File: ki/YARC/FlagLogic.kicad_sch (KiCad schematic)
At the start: 11 parts, among them U105 74LS86, U106 74LS139, U107 74HC00, U108 74HC02, U109 74LS32, U110 74LS21, U111 74LS153, U112 74LS573, U113 74LS573, U114 74LS574, U115 74LS574

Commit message: Various corrections and minor improvements
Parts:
- removed unit 4 of U107
- removed unit 3 of U107
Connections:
- net GND: now also U107.1; no longer U107.4, U107.5
- net IRH2: now also U107.4, U107.5; no longer U107.1, U107.2
- net at U111.1 (Ea): now also U107.6; no longer U107.3
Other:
- moved on the sheet: U107A
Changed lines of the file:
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@@
   (junction (at 40.64 119.38) (diameter 0) (color 0 0 0 0)
   )
-  (junction (at 33.02 172.72) (diameter 0) (color 0 0 0 0)
-  )
   (junction (at 86.36 165.1) (diameter 0) (color 0 0 0 0)
   )
@@
   (junction (at 76.2 172.72) (diameter 0) (color 0 0 0 0)
   )
-  (junction (at 33.02 180.34) (diameter 0) (color 0 0 0 0)
-  )
   (junction (at 30.48 45.72) (diameter 0) (color 0 0 0 0)
   )
   (junction (at 73.66 147.32) (diameter 0) (color 0 0 0 0)
   )
-  (junction (at 30.48 193.04) (diameter 0) (color 0 0 0 0)
-  )
   (junction (at 86.36 160.02) (diameter 0) (color 0 0 0 0)
   )
   (junction (at 53.34 147.32) (diameter 0) (color 0 0 0 0)
   )
-  (junction (at 50.8 193.04) (diameter 0) (color 0 0 0 0)
-  )
   (junction (at 121.92 172.72) (diameter 0) (color 0 0 0 0)
   )
@@
   (junction (at 33.02 48.26) (diameter 0) (color 0 0 0 0)
   )
-  (junction (at 50.8 172.72) (diameter 0) (color 0 0 0 0)
-  )
   (junction (at 76.2 193.04) (diameter 0) (color 0 0 0 0)
   )
@@
     (stroke (width 0) (type default) (color 0 0 0 0))
   )
-  (wire (pts (xy 30.48 198.12) (xy 30.48 193.04))
-    (stroke (width 0) (type default) (color 0 0 0 0))
-  )
   (bus (pts (xy 172.72 22.86) (xy 190.5 22.86))
     (stroke (width 0) (type default) (color 0 0 0 0))
@@
     (stroke (width 0) (type default) (color 0 0 0 0))
   )
-  (wire (pts (xy 30.48 193.04) (xy 30.48 172.72))
-    (stroke (width 0) (type default) (color 0 0 0 0))
-  )
   (wire (pts (xy 241.3 73.66) (xy 241.3 60.96))
     (stroke (width 0) (type default) (color 0 0 0 0))
@@
     (stroke (width 0) (type default) (color 0 0 0 0))
   )
-  (wire (pts (xy 30.48 172.72) (xy 33.02 172.72))
+  (wire (pts (xy 30.48 172.72) (xy 35.56 172.72))
     (stroke (width 0) (type default) (color 0 0 0 0))
   )
@@
     (stroke (width 0) (type default) (color 0 0 0 0))
   )
-  (wire (pts (xy 50.8 198.12) (xy 50.8 193.04))
-    (stroke (width 0) (type default) (color 0 0 0 0))
-  )
   (wire (pts (xy 25.4 119.38) (xy 40.64 119.38))
     (stroke (width 0) (type default) (color 0 0 0 0))
   )
+  (wire (pts (xy 30.48 180.34) (xy 30.48 172.72))
+    (stroke (width 0) (type default) (color 0 0 0 0))
+  )
   (wire (pts (xy 104.14 93.98) (xy 109.22 93.98))
     (stroke (width 0) (type default) (color 0 0 0 0))
   )
-  (wire (pts (xy 33.02 180.34) (xy 33.02 172.72))
-    (stroke (width 0) (type default) (color 0 0 0 0))
-  )
   (wire (pts (xy 73.66 172.72) (xy 76.2 172.72))
     (stroke (width 0) (type default) (color 0 0 0 0))
@@
     (stroke (width 0) (type default) (color 0 0 0 0))
   )
-  (wire (pts (xy 33.02 185.42) (xy 33.02 180.34))
-    (stroke (width 0) (type default) (color 0 0 0 0))
-  )
   (bus (pts (xy 228.6 88.9) (xy 246.38 88.9))
     (stroke (width 0) (type default) (color 0 0 0 0))
@@
     (stroke (width 0) (type default) (color 0 0 0 0))
   )
-  (wire (pts (xy 35.56 172.72) (xy 50.8 172.72))
+  (wire (pts (xy 35.56 172.72) (xy 53.34 172.72))
     (stroke (width 0) (type default) (color 0 0 0 0))
   )
@@
     (stroke (width 0) (type default) (color 0 0 0 0))
   )
-  (wire (pts (xy 50.8 193.04) (xy 50.8 172.72))
-    (stroke (width 0) (type default) (color 0 0 0 0))
-  )
   (wire (pts (xy 170.18 73.66) (xy 170.18 60.96))
     (stroke (width 0) (type default) (color 0 0 0 0))
@@
     (stroke (width 0) (type default) (color 0 0 0 0))
   )
-  (wire (pts (xy 50.8 172.72) (xy 53.34 172.72))
-    (stroke (width 0) (type default) (color 0 0 0 0))
-  )
   (wire (pts (xy 19.05 147.32) (xy 35.56 147.32))
     (stroke (width 0) (type default) (color 0 0 0 0))
@@
   )
   (bus (pts (xy 22.86 99.06) (xy 22.86 104.14))
-    (stroke (width 0) (type default) (color 0 0 0 0))
-  )
-  (wire (pts (xy 33.02 172.72) (xy 35.56 172.72))
     (stroke (width 0) (type default) (color 0 0 0 0))
   )
@@
     (pin "3")
   )
-  (symbol (lib_id "74xx:74HC00") (at 38.1 195.58 0) (unit 2)
-    (in_bom yes) (on_board yes)
-    (property "Reference" "U107" (id 0) (at 43.18 190.5 0))
-    (property "Value" "74HC00" (id 1) (at 38.1 195.58 0))
-    (property "Footprint" "" (id 2) (at 38.1 195.58 0)
-      (effects (font (size 1.27 1.27)) hide)
-    )
-    (property "Datasheet" "http://www.ti.com/lit/gpn/sn74hc00" (id 3) (at 38.1 195.58 0)
-      (effects (font (size 1.27 1.27)) hide)
-    )
-    (pin "4")
-    (pin "5")
-    (pin "6")
+  (symbol (lib_id "74xx:74HC00") (at 38.1 182.88 0) (unit 1)
+    (in_bom yes) (on_board yes)
+    (property "Reference" "U107" (id 0) (at 43.18 177.8 0))
+    (property "Value" "74HC00" (id 1) (at 38.1 182.88 0))
+    (property "Footprint" "" (id 2) (at 38.1 182.88 0)
+      (effects (font (size 1.27 1.27)) hide)
+    )
+    (property "Datasheet" "http://www.ti.com/lit/gpn/sn74hc00" (id 3) (at 38.1 182.88 0)
+      (effects (font (size 1.27 1.27)) hide)
+    )
+    (pin "1")
+    (pin "2")
+    (pin "3")
   )
   (symbol (lib_id "74xx:74HC02") (at 83.82 195.58 0) (unit 1)
@@
     (pin "9")
   )
-  (symbol (lib_id "74xx:74HC00") (at 53.34 73.66 0) (unit 1)
+  (symbol (lib_id "74xx:74HC00") (at 53.34 73.66 0) (unit 2)
     (in_bom yes) (on_board yes)
     (property "Reference" "U107" (id 0) (at 58.42 68.58 0))
@@
       (effects (font (size 1.27 1.27)) hide)
     )
-    (pin "1")
-    (pin "2")
-    (pin "3")
+    (pin "4")
+    (pin "5")
+    (pin "6")
   )
   (symbol (lib_id "74xx:74LS32") (at 129.54 60.96 270) (unit 2)
@@
     (pin "1")
   )
-  (symbol (lib_id "74xx:74HC00") (at 58.42 195.58 0) (unit 4)
-    (in_bom yes) (on_board yes)
-    (property "Reference" "U107" (id 0) (at 63.5 190.5 0))
-    (property "Value" "74HC00" (id 1) (at 58.42 195.58 0))
-    (property "Footprint" "" (id 2) (at 58.42 195.58 0)
-      (effects (font (size 1.27 1.27)) hide)
-    )
-    (property "Datasheet" "http://www.ti.com/lit/gpn/sn74hc00" (id 3) (at 58.42 195.58 0)
-      (effects (font (size 1.27 1.27)) hide)
-    )
-    (pin "11")
-    (pin "12")
-    (pin "13")
-  )
   (symbol (lib_id "74xx:74LS32") (at 73.66 160.02 0) (unit 5)
     (in_bom yes) (on_board yes)
@@
     (pin "1")
   )
-  (symbol (lib_id "74xx:74HC00") (at 40.64 182.88 0) (unit 3)
-    (in_bom yes) (on_board yes)
-    (property "Reference" "U107" (id 0) (at 45.72 177.8 0))
-    (property "Value" "74HC00" (id 1) (at 40.64 182.88 0))
-    (property "Footprint" "" (id 2) (at 40.64 182.88 0)
-      (effects (font (size 1.27 1.27)) hide)
-    )
-    (property "Datasheet" "http://www.ti.com/lit/gpn/sn74hc00" (id 3) (at 40.64 182.88 0)
-      (effects (font (size 1.27 1.27)) hide)
-    )
-    (pin "10")
-    (pin "8")
-    (pin "9")
-  )
   (symbol (lib_id "power:VCC") (at 139.7 147.32 0) (unit 1)

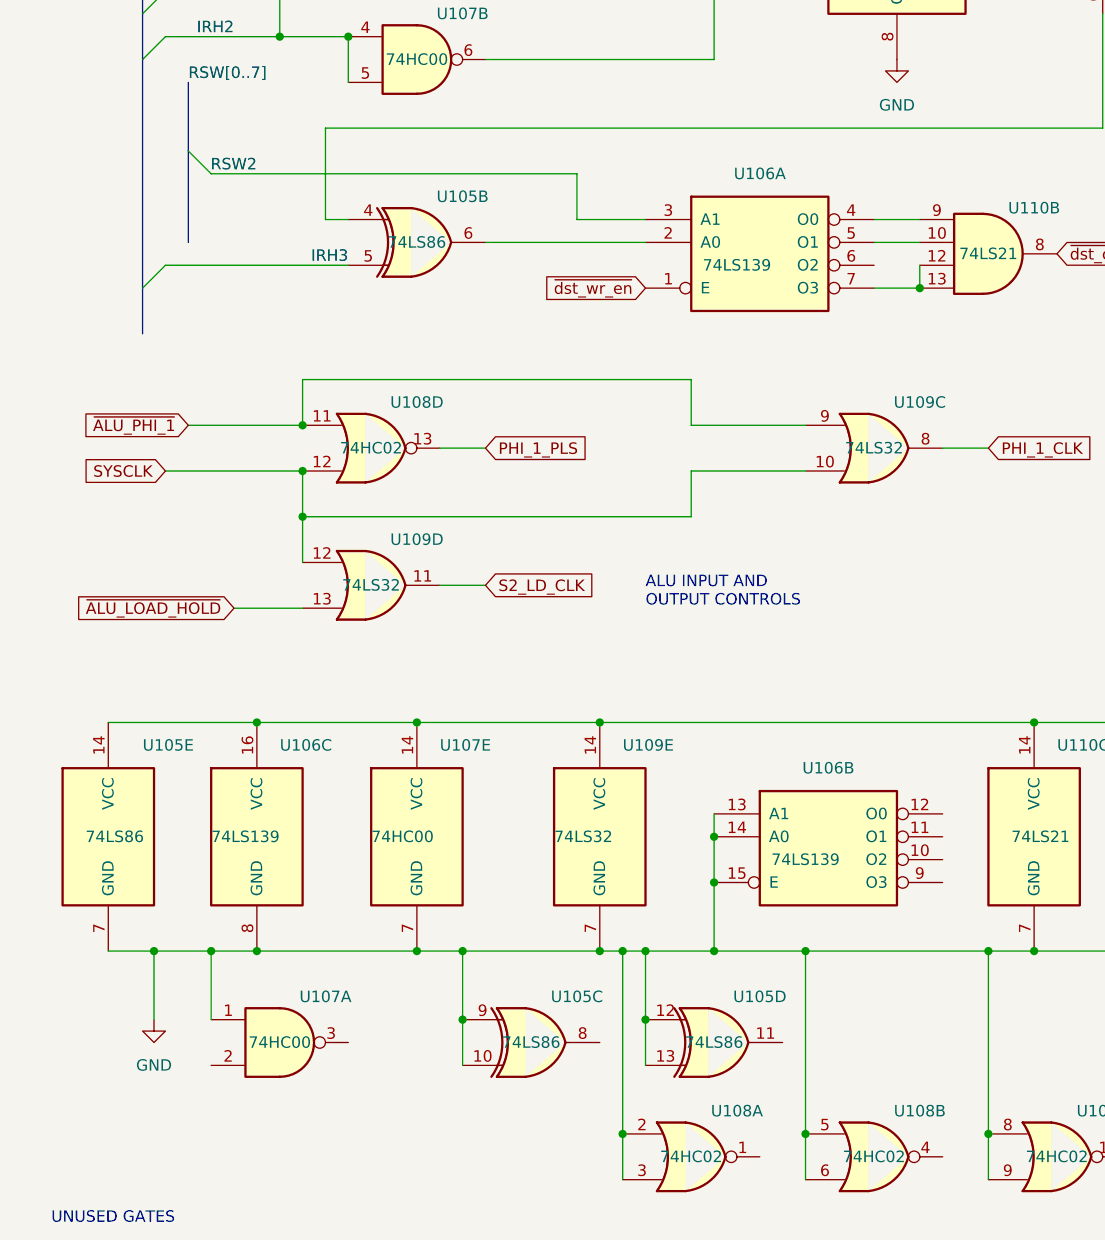
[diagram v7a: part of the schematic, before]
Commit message: Redesign of ALU control logic
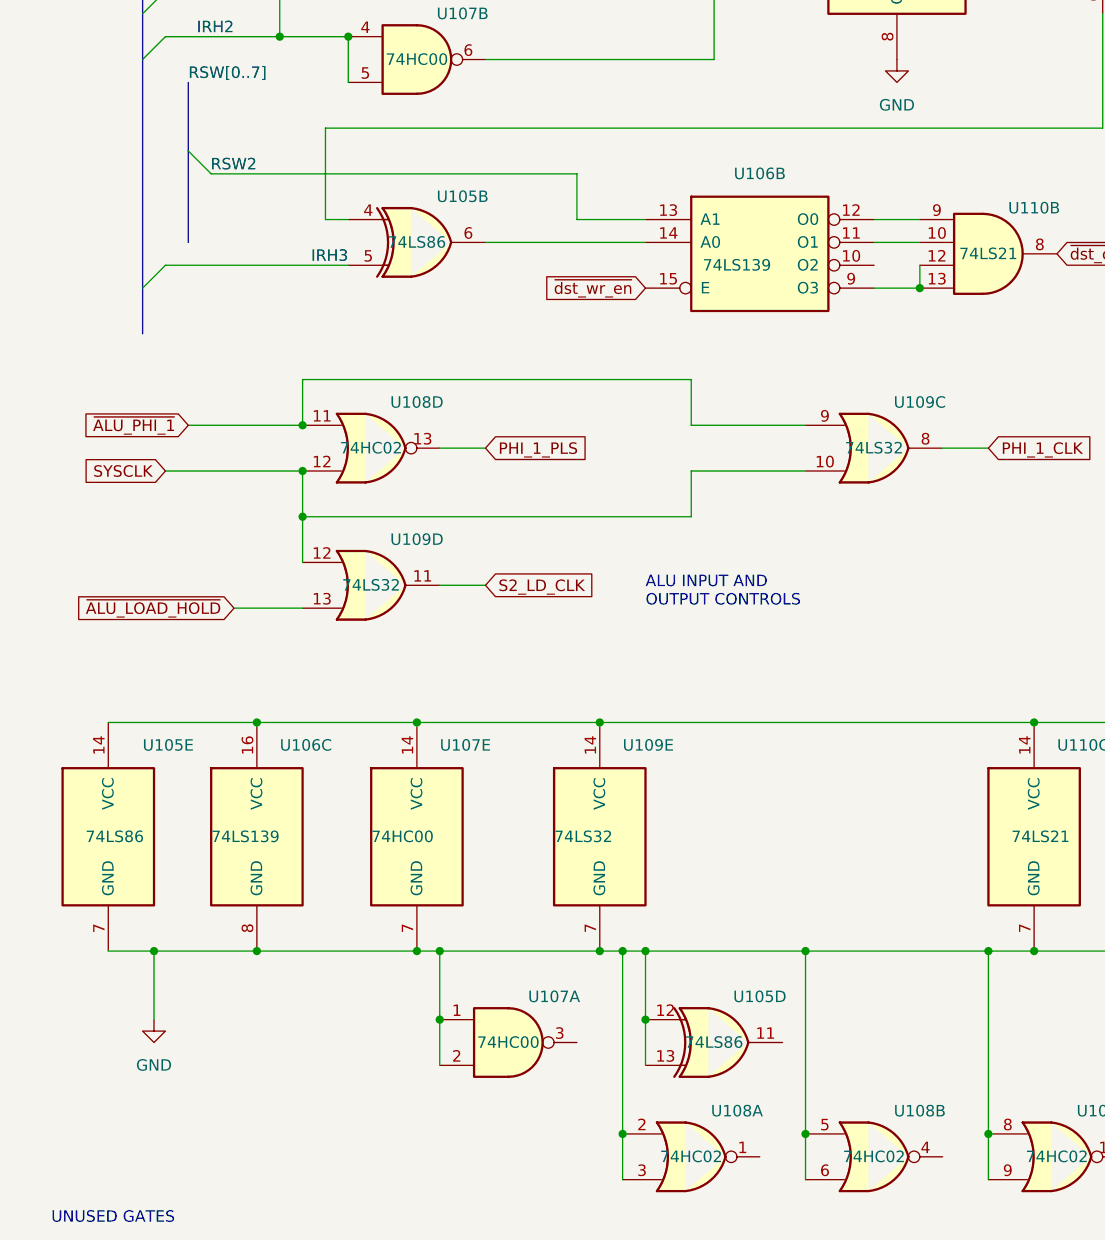
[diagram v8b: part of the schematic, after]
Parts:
- removed unit 3 of U105
- removed unit 2 of U106
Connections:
- net GND: now also U107.2
- net RSW2: now also U106.13 (A1); no longer U106.3 (A1)
- net ~{dst_wr_en}: now also U106.15 (E); no longer U106.1 (E)
- net at U105.6: now also U106.14 (A0); no longer U106.2 (A0)
- net at U110.10: now also U106.11 (O1); no longer U106.5 (O1)
- net at U110.12, U110.13: now also U106.9 (O3); no longer U106.7 (O3)
- net at U110.9: now also U106.12 (O0); no longer U106.4 (O0)
